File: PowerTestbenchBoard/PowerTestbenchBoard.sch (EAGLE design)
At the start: 42 parts, among them J3 POWER_JACK, J5 POWER_JACK, J8 182-037-213R531, J9 182-025-213R531

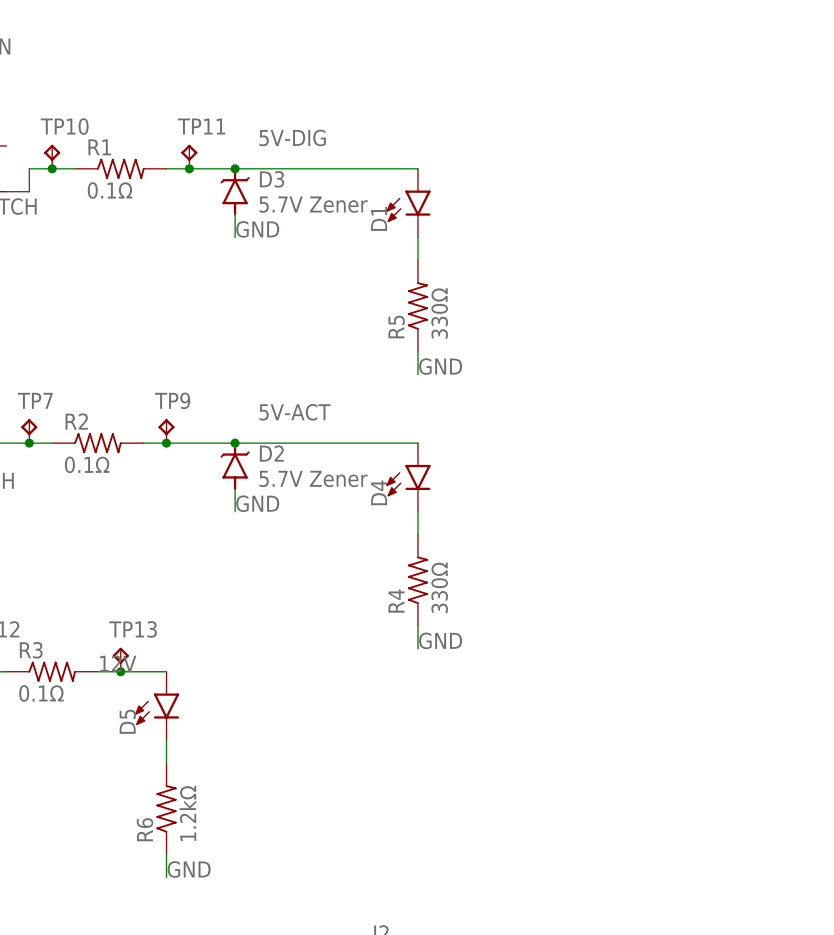
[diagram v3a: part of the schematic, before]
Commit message: Added caps on power busses. Enlarged power traces
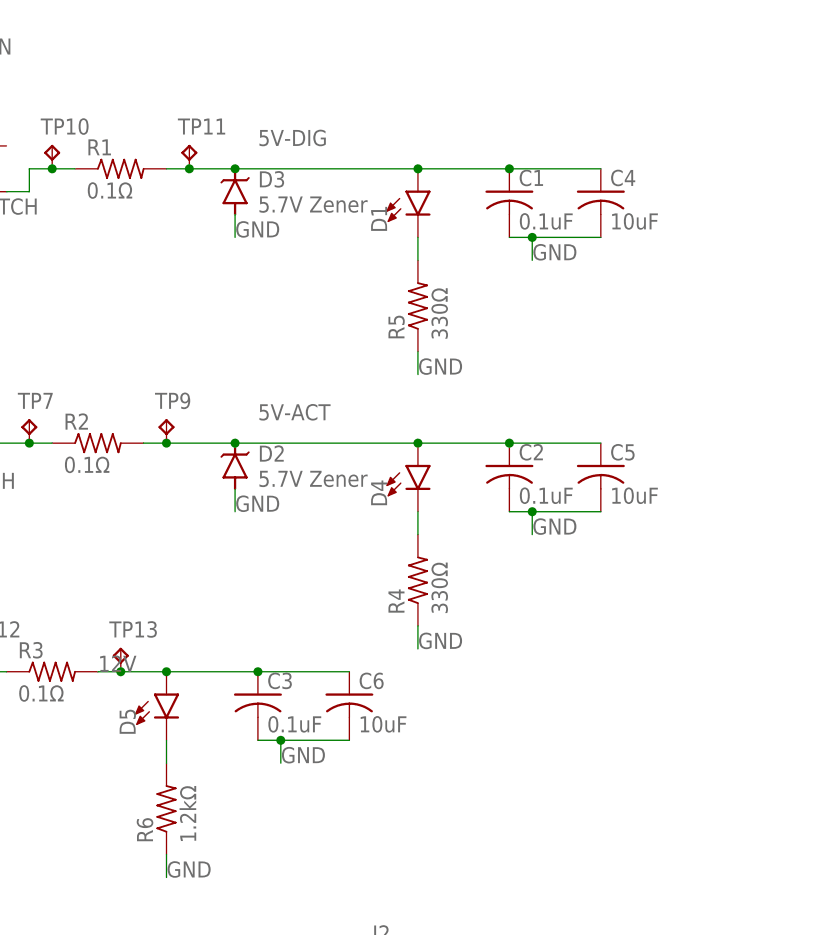
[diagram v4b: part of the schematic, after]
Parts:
- added C1, C2, C3: 0.1uF, rcl:C-USC0805
- added C4, C5, C6: 10uF, rcl:C-USC0805
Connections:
- net 12V: now also C3.1, C6.1
- net 5V-ACT: now also C2.1, C5.1
- net 5V-DIG: now also C1.1, C4.1
- net GND: now also C1.2, C2.2, C3.2, C4.2, C5.2, C6.2
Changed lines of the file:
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@@
 <part name="R5" library="rcl" library_urn="urn:adsk.eagle:library:334" deviceset="R-US_" device="R0805" package3d_urn="urn:adsk.eagle:package:23553/2" value="330Ω"/>
 <part name="R6" library="rcl" library_urn="urn:adsk.eagle:library:334" deviceset="R-US_" device="R0805" package3d_urn="urn:adsk.eagle:package:23553/2" value="1.2kΩ"/>
+<part name="C1" library="rcl" library_urn="urn:adsk.eagle:library:334" deviceset="C-US" device="C0805" package3d_urn="urn:adsk.eagle:package:23617/2" value="0.1uF"/>
+<part name="C2" library="rcl" library_urn="urn:adsk.eagle:library:334" deviceset="C-US" device="C0805" package3d_urn="urn:adsk.eagle:package:23617/2" value="0.1uF"/>
+<part name="C3" library="rcl" library_urn="urn:adsk.eagle:library:334" deviceset="C-US" device="C0805" package3d_urn="urn:adsk.eagle:package:23617/2" value="0.1uF"/>
+<part name="C4" library="rcl" library_urn="urn:adsk.eagle:library:334" deviceset="C-US" device="C0805" package3d_urn="urn:adsk.eagle:package:23617/2" value="10uF"/>
+<part name="C5" library="rcl" library_urn="urn:adsk.eagle:library:334" deviceset="C-US" device="C0805" package3d_urn="urn:adsk.eagle:package:23617/2" value="10uF"/>
+<part name="C6" library="rcl" library_urn="urn:adsk.eagle:library:334" deviceset="C-US" device="C0805" package3d_urn="urn:adsk.eagle:package:23617/2" value="10uF"/>
 </parts>
 <sheets>
@@
 <attribute name="VALUE" x="71.882" y="62.23" size="1.778" layer="96" rot="R90"/>
 </instance>
+<instance part="C1" gate="G$1" x="106.68" y="134.62" smashed="yes">
+<attribute name="NAME" x="107.696" y="135.255" size="1.778" layer="95"/>
+<attribute name="VALUE" x="107.696" y="130.429" size="1.778" layer="96"/>
+</instance>
+<instance part="C2" gate="G$1" x="106.68" y="104.14" smashed="yes">
+<attribute name="NAME" x="107.696" y="104.775" size="1.778" layer="95"/>
+<attribute name="VALUE" x="107.696" y="99.949" size="1.778" layer="96"/>
+</instance>
+<instance part="C3" gate="G$1" x="78.74" y="78.74" smashed="yes">
+<attribute name="NAME" x="79.756" y="79.375" size="1.778" layer="95"/>
+<attribute name="VALUE" x="79.756" y="74.549" size="1.778" layer="96"/>
+</instance>
+<instance part="C4" gate="G$1" x="116.84" y="134.62" smashed="yes">
+<attribute name="NAME" x="117.856" y="135.255" size="1.778" layer="95"/>
+<attribute name="VALUE" x="117.856" y="130.429" size="1.778" layer="96"/>
+</instance>
+<instance part="C5" gate="G$1" x="116.84" y="104.14" smashed="yes">
+<attribute name="NAME" x="117.856" y="104.775" size="1.778" layer="95"/>
+<attribute name="VALUE" x="117.856" y="99.949" size="1.778" layer="96"/>
+</instance>
+<instance part="C6" gate="G$1" x="88.9" y="78.74" smashed="yes">
+<attribute name="NAME" x="89.916" y="79.375" size="1.778" layer="95"/>
+<attribute name="VALUE" x="89.916" y="74.549" size="1.778" layer="96"/>
+</instance>
 </instances>
 <busses>
@@
 <wire x1="63.5" y1="12.7" x2="66.04" y2="12.7" width="0.1524" layer="91"/>
 <label x="66.04" y="12.7" size="1.778" layer="95"/>
+</segment>
+<segment>
+<pinref part="C3" gate="G$1" pin="2"/>
+<pinref part="C6" gate="G$1" pin="2"/>
+<wire x1="78.74" y1="73.66" x2="81.28" y2="73.66" width="0.1524" layer="91"/>
+<wire x1="81.28" y1="73.66" x2="88.9" y2="73.66" width="0.1524" layer="91"/>
+<wire x1="81.28" y1="73.66" x2="81.28" y2="71.12" width="0.1524" layer="91"/>
+<junction x="81.28" y="73.66"/>
+<label x="81.28" y="71.12" size="1.778" layer="95"/>
+</segment>
+<segment>
+<pinref part="C2" gate="G$1" pin="2"/>
+<pinref part="C5" gate="G$1" pin="2"/>
+<wire x1="106.68" y1="99.06" x2="109.22" y2="99.06" width="0.1524" layer="91"/>
+<wire x1="109.22" y1="99.06" x2="116.84" y2="99.06" width="0.1524" layer="91"/>
+<wire x1="109.22" y1="99.06" x2="109.22" y2="96.52" width="0.1524" layer="91"/>
+<junction x="109.22" y="99.06"/>
+<label x="109.22" y="96.52" size="1.778" layer="95"/>
+</segment>
+<segment>
+<pinref part="C1" gate="G$1" pin="2"/>
+<pinref part="C4" gate="G$1" pin="2"/>
+<wire x1="106.68" y1="129.54" x2="109.22" y2="129.54" width="0.1524" layer="91"/>
+<wire x1="109.22" y1="129.54" x2="116.84" y2="129.54" width="0.1524" layer="91"/>
+<wire x1="109.22" y1="129.54" x2="109.22" y2="127" width="0.1524" layer="91"/>
+<junction x="109.22" y="129.54"/>
+<label x="109.22" y="127" size="1.778" layer="95"/>
 </segment>
 </net>
@@
 <wire x1="76.2" y1="137.16" x2="96.52" y2="137.16" width="0.1524" layer="91"/>
 <junction x="76.2" y="137.16"/>
+<pinref part="C1" gate="G$1" pin="1"/>
+<pinref part="C4" gate="G$1" pin="1"/>
+<wire x1="106.68" y1="137.16" x2="116.84" y2="137.16" width="0.1524" layer="91"/>
+<wire x1="106.68" y1="137.16" x2="96.52" y2="137.16" width="0.1524" layer="91"/>
+<junction x="106.68" y="137.16"/>
+<junction x="96.52" y="137.16"/>
 </segment>
 <segment>
@@
 <wire x1="76.2" y1="106.68" x2="96.52" y2="106.68" width="0.1524" layer="91"/>
 <junction x="76.2" y="106.68"/>
+<pinref part="C2" gate="G$1" pin="1"/>
+<wire x1="96.52" y1="106.68" x2="106.68" y2="106.68" width="0.1524" layer="91"/>
+<junction x="96.52" y="106.68"/>
+<pinref part="C5" gate="G$1" pin="1"/>
+<wire x1="106.68" y1="106.68" x2="116.84" y2="106.68" width="0.1524" layer="91"/>
+<junction x="106.68" y="106.68"/>
 </segment>
 </net>
@@
 <wire x1="68.58" y1="81.28" x2="63.5" y2="81.28" width="0.1524" layer="91"/>
 <junction x="63.5" y="81.28"/>
-</segment>
-</net>
+<pinref part="C3" gate="G$1" pin="1"/>
+<wire x1="68.58" y1="81.28" x2="78.74" y2="81.28" width="0.1524" layer="91"/>
+<junction x="68.58" y="81.28"/>
+<pinref part="C6" gate="G$1" pin="1"/>
+<wire x1="78.74" y1="81.28" x2="88.9" y2="81.28" width="0.1524" layer="91"/>
+<junction x="78.74" y="81.28"/>
+</segment>
+</net>

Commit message: Added jumper
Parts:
- added JP1: (no value), jumper:JP1E
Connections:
- net 5V-ACT-IN: now also JP1.1
- net 5V-DIG-IN: now also JP1.2
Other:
- note added: "Option to Connect 5V-Dig-In and 5V-Act-In together"
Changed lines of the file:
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@@
 <part name="C5" library="rcl" library_urn="urn:adsk.eagle:library:334" deviceset="C-US" device="C0805" package3d_urn="urn:adsk.eagle:package:23617/2" value="10uF"/>
 <part name="C6" library="rcl" library_urn="urn:adsk.eagle:library:334" deviceset="C-US" device="C0805" package3d_urn="urn:adsk.eagle:package:23617/2" value="10uF"/>
+<part name="JP1" library="jumper" library_urn="urn:adsk.eagle:library:252" deviceset="JP1E" device="" package3d_urn="urn:adsk.eagle:package:15455/1"/>
 </parts>
 <sheets>
@@
 <text x="142.24" y="165.1" size="1.778" layer="97">Conn to Data Control Board</text>
 <text x="223.52" y="172.72" size="1.778" layer="97">Conn to Experiments</text>
+<text x="124.46" y="71.12" size="1.778" layer="97">Option to Connect 5V-Dig-In and 5V-Act-In together</text>
 </plain>
 <instances>
@@
 <attribute name="NAME" x="89.916" y="79.375" size="1.778" layer="95"/>
 <attribute name="VALUE" x="89.916" y="74.549" size="1.778" layer="96"/>
+</instance>
+<instance part="JP1" gate="A" x="144.78" y="63.5" smashed="yes" rot="R90">
+<attribute name="NAME" x="144.78" y="62.23" size="1.778" layer="95" rot="R180"/>
+<attribute name="VALUE" x="144.78" y="69.215" size="1.778" layer="96" rot="R180"/>
 </instance>
 </instances>
@@
 <label x="142.24" y="35.56" size="1.778" layer="95" rot="R180"/>
 </segment>
+<segment>
+<pinref part="JP1" gate="A" pin="2"/>
+<wire x1="147.32" y1="66.04" x2="149.86" y2="66.04" width="0.1524" layer="91"/>
+<wire x1="149.86" y1="66.04" x2="149.86" y2="68.58" width="0.1524" layer="91"/>
+<wire x1="149.86" y1="68.58" x2="152.4" y2="68.58" width="0.1524" layer="91"/>
+<label x="152.4" y="68.58" size="1.778" layer="95"/>
+</segment>
 </net>
 <net name="5V-ACT-IN" class="0">
@@
 <label x="142.24" y="30.48" size="1.778" layer="95" rot="R180"/>
 </segment>
-</net>
+<segment>
+<pinref part="JP1" gate="A" pin="1"/>
+<wire x1="147.32" y1="63.5" x2="149.86" y2="63.5" width="0.1524" layer="91"/>
+<wire x1="149.86" y1="63.5" x2="149.86" y2="60.96" width="0.1524" layer="91"/>
+<wire x1="149.86" y1="60.96" x2="152.4" y2="60.96" width="0.1524" layer="91"/>
+<label x="152.4" y="60.96" size="1.778" layer="95"/>
+</segment>
+</net>
